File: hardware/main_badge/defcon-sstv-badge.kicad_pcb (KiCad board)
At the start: 4 copper layers, 185.7 x 199 mm, 136 parts, among them J1 Conn_01x02, J10 Micro_SD_Card, J11 Mechanical/Grounds, J12 Mechanical/Grounds, J2 USB4105-GF-A, J3 ILI9341 Display Module, J4 Conn_02x09_Odd_Even, J5 SAO1, J6 SAO2, J7 Conn_01x08_Socket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

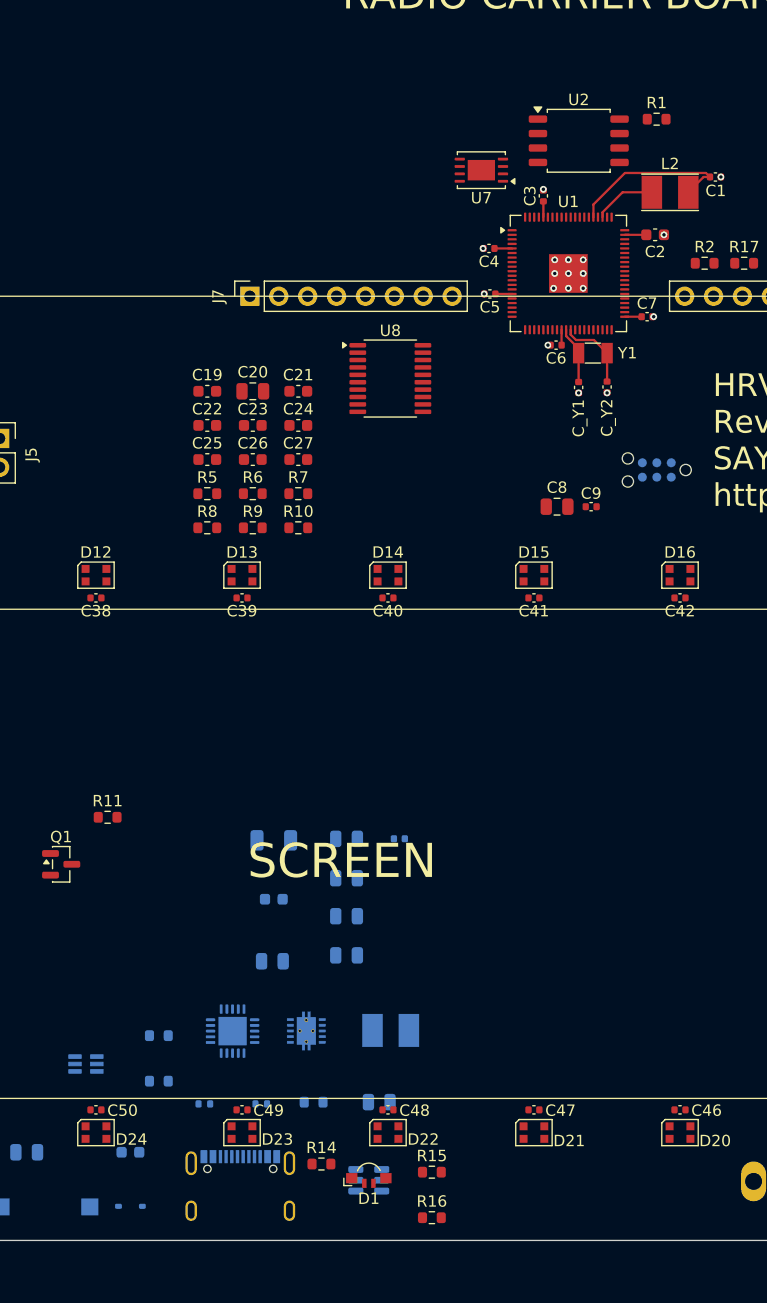
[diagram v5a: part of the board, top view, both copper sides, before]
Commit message: USB port and chip routed
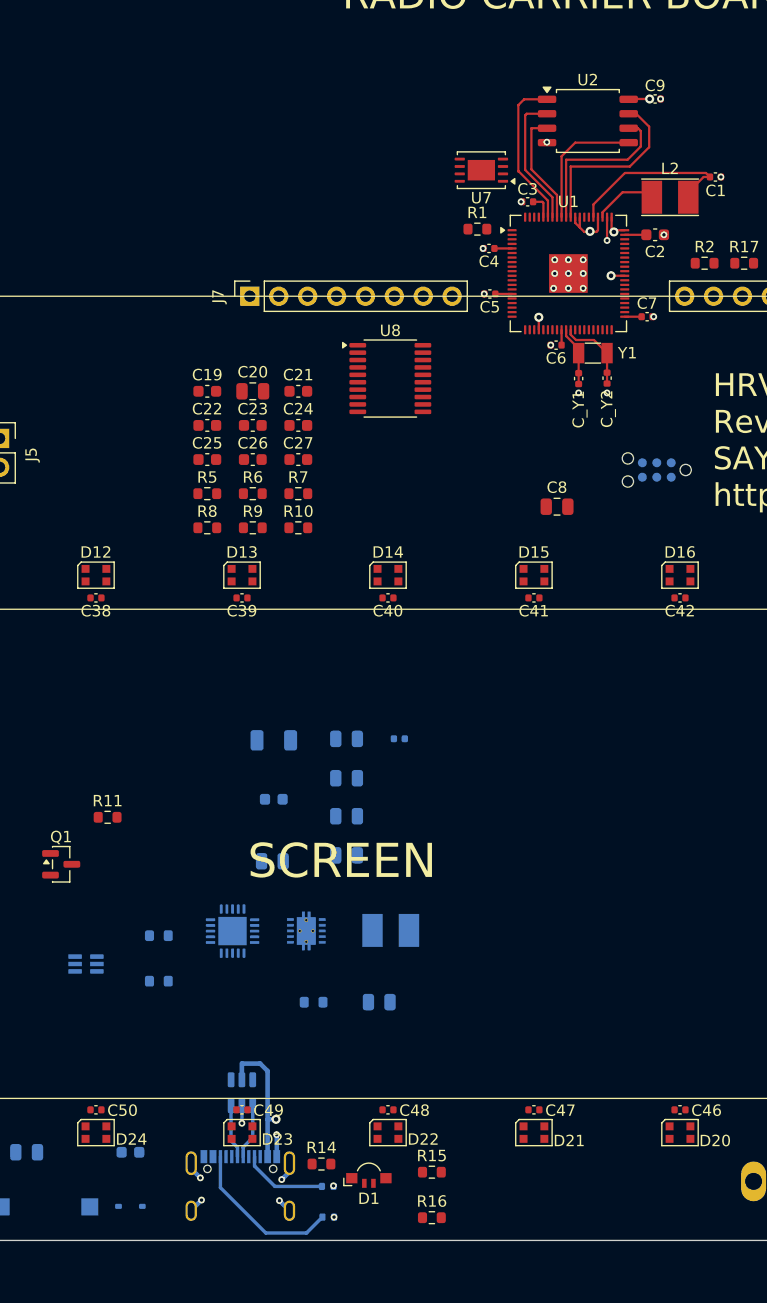
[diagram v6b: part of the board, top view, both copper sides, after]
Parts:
- moved C9 36.3 mm to (67.6, 19.7)
- moved R1 18.5 mm to (52.0, 31.1)
- moved R_CC2 14.8 mm to (38.9, 118.0), turned to 0 degrees
- moved U3 13.6 mm to (31.3, 107.0), turned to 90 degrees
- moved R_CC1 9.32 mm to (38.9, 115.2)
- moved C10 8.79 mm to (43.4, 99.0)
- moved C12 8.79 mm to (40.5, 75.9)
- moved C14 8.79 mm to (40.5, 82.7)
- moved C18 8.79 mm to (34.1, 81.2)
- moved L1 8.79 mm to (44.4, 92.8)
- moved R3 8.79 mm to (24.0, 93.2)
- moved R4 8.79 mm to (24.0, 97.2)
- moved U5 8.79 mm to (37.0, 92.8)
- moved C13 8.79 mm to (40.5, 79.4)
- moved C15 8.79 mm to (40.5, 86.2)
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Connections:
- U1 pad 74: Net-(U1-QSPI_SD0) -> Net-(U1-QSPI_SD1)
- U2 pad 2: Net-(U1-QSPI_SD0) -> Net-(U1-QSPI_SD1)
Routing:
- net Net-(U1-QSPI_SD3): track 0.00 -> 16.1 mm
- net Net-(U1-QSPI_SCLK): track 0.00 -> 14.6 mm
- net Net-(J2-CC2): track 0.00 -> 13.9 mm
- net Net-(U1-~{QSPI_SS}): track 0.00 -> 13.7 mm
- net +3V3: track 9.44 -> 22.1 mm, vias 0 -> 5
- net VBUS: track 0.00 -> 12.2 mm, vias 0 -> 1
- net Net-(U1-QSPI_SD1): track 0.00 -> 11.9 mm
- net Net-(U1-QSPI_SD0): track 0.00 -> 11.7 mm
- net GND: track 11.9 -> 23.6 mm, vias 18 -> 29
- net Net-(U1-QSPI_SD2): track 0.00 -> 10.1 mm
- net Net-(J2-CC1): track 0.00 -> 7.50 mm
- net Net-(J2-DP1): track 0.00 -> 4.83 mm
- net Net-(J2-DN1): track 0.00 -> 4.72 mm

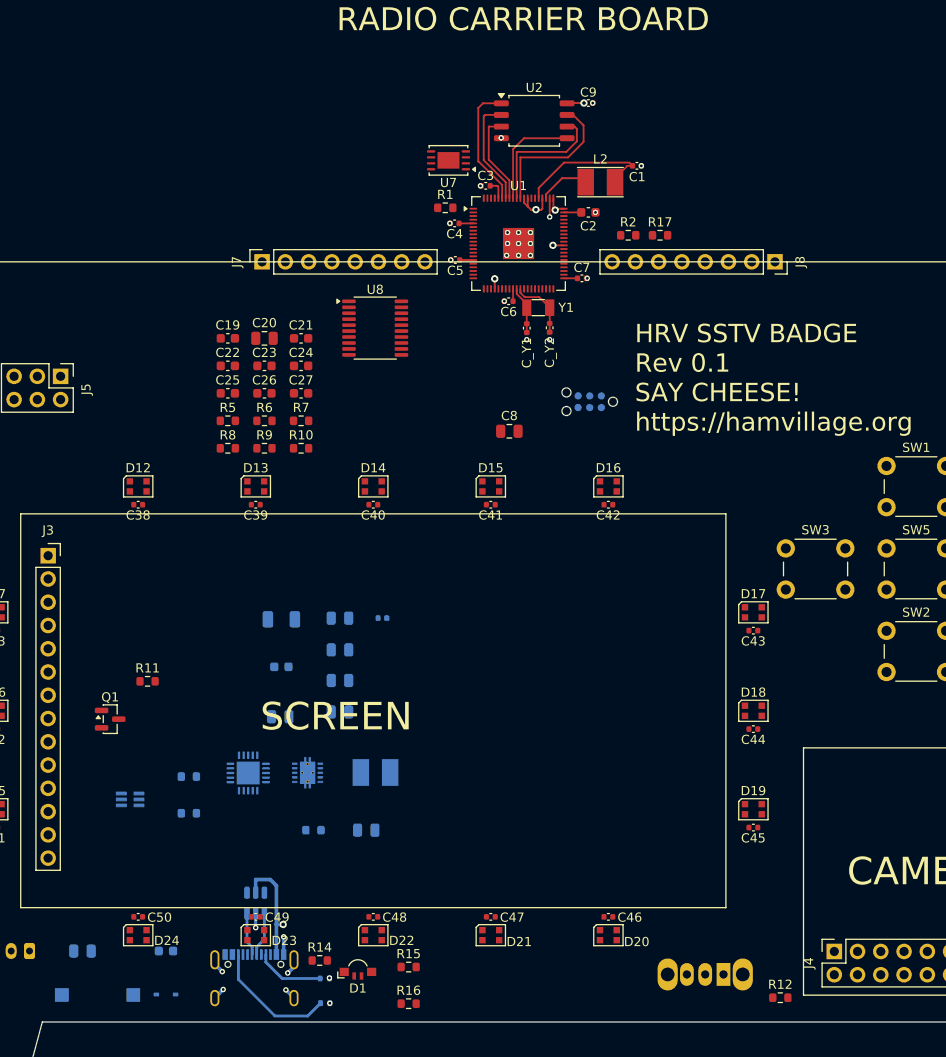
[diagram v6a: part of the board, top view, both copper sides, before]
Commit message: U5 routing complete
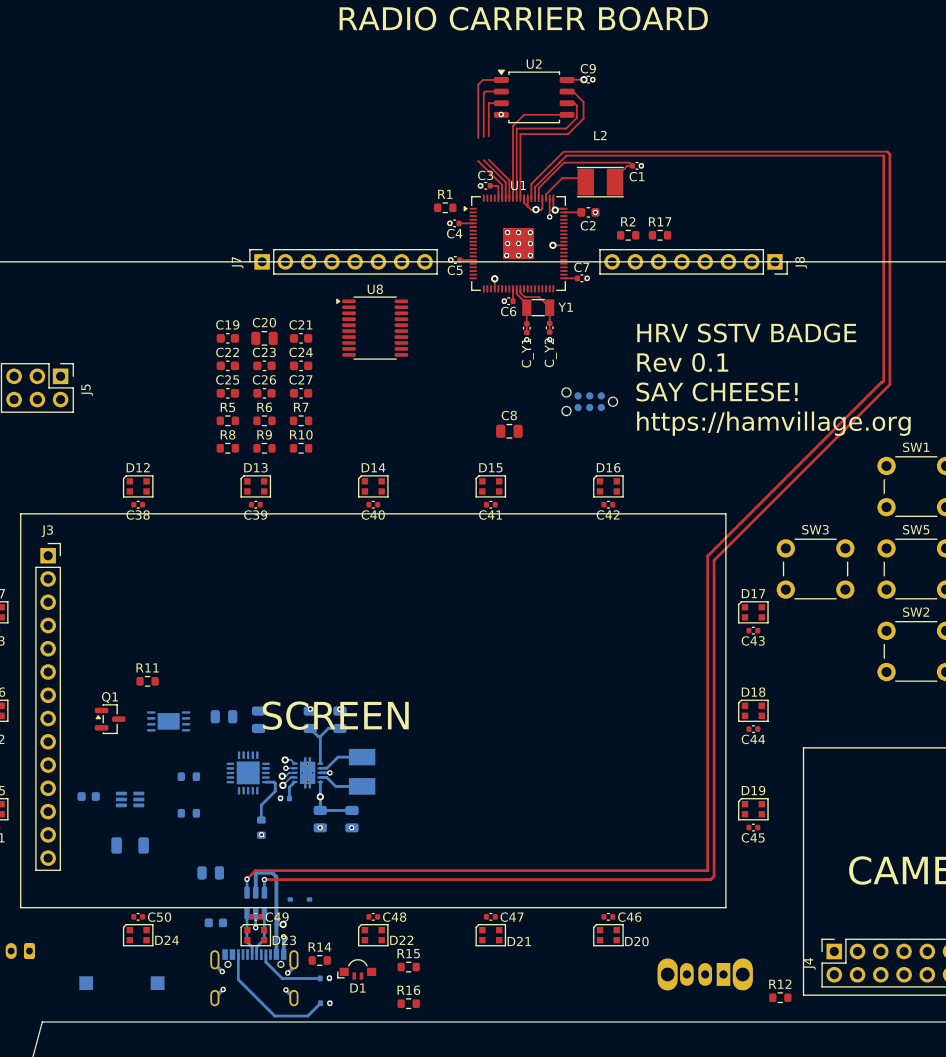
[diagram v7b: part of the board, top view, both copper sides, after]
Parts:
- U7: moved to B.Cu
- moved U7 68.5 mm to (21.8, 87.2), turned to 0 degrees
- moved C11 29.9 mm to (27.8, 86.7)
- moved C17 29.7 mm to (17.6, 100.7), turned to 0 degrees
- moved C18 25.4 mm to (13.1, 95.4)
- moved C16 22.4 mm to (34.5, 95.6)
- moved C12 22.0 mm to (38.4, 97.8), turned to -90 degrees
- moved C13 18.5 mm to (41.8, 97.8), turned to 90 degrees
- moved D_VBUS1 17.9 mm to (36.1, 106.6)
- moved C10 17.6 mm to (26.4, 103.7)
- moved C_USB1 6.26 mm to (26.9, 109.2), turned to 0 degrees
- moved TH1 5.69 mm to (31.9, 98.8), turned to 90 degrees
- moved C14 4.29 mm to (40.5, 87.0), turned to 90 degrees
- moved C15 3.35 mm to (37.3, 87.0), turned to 90 degrees
- moved SW_BOOT1 2.96 mm to (16.7, 115.8)
- moved C9 2.55 mm to (67.6, 17.1)
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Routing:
- net USB_DP: track 0.00 -> 179.7 mm, vias 0 -> 1
- net USB_DM: track 0.00 -> 179.0 mm, vias 0 -> 1
- net VSYS: track 0.00 -> 10.7 mm, vias 0 -> 2
- net +3V3: track 22.1 -> 32.7 mm, vias 5 -> 7
- net Net-(U4-THERM): track 0.00 -> 5.71 mm
- net Net-(U5-L2): track 0.00 -> 5.06 mm
- net Net-(U5-L1): track 0.00 -> 4.97 mm
- net Net-(U1-QSPI_SD3): track 16.1 -> 18.7 mm
- net Net-(U1-QSPI_SD0): track 11.7 -> 14.3 mm
- net Net-(U1-QSPI_SCLK): track 14.6 -> 17.2 mm
- net GND: track 23.6 -> 25.8 mm, vias 29 -> 37
- net VBUS: track 12.2 -> 13.8 mm

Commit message: work in progress power subsystems routing
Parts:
- moved U7 6.36 mm to (16.6, 90.9)
- moved R4 3.07 mm to (25.4, 94.5), turned to 0 degrees
- moved C15 2.19 mm to (39.5, 87.0)
- moved C16 2.19 mm to (36.7, 95.6)
- moved C12 2.19 mm to (40.5, 97.8)
- moved C13 2.19 mm to (44.0, 97.8)
- moved C14 2.19 mm to (42.7, 87.0)
- moved L1 2.19 mm to (45.1, 92.7)
- moved U5 2.19 mm to (39.1, 92.8)
- moved R3 1.41 mm to (25.4, 92.8)
- moved C11 0.37 mm to (28.0, 87.0), turned to -90 degrees
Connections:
- J1 pad 2: VSYS -> GND
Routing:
- net Net-(J1-Pin_1): track 0.00 -> 53.7 mm
- net GND: track 25.8 -> 46.4 mm, vias 37 -> 45
- net Net-(U4-THERM): track 5.71 -> 22.1 mm
- net Net-(C11-Pad2): track 0.00 -> 10.5 mm
- net VBUS: track 13.8 -> 21.7 mm, vias 1 -> 5
- net VSYS: track 10.7 -> 13.6 mm, vias 2 -> 5
- net Net-(U4-PROG3): track 0.00 -> 2.84 mm
- net Net-(U4-PROG1): track 0.00 -> 2.36 mm
